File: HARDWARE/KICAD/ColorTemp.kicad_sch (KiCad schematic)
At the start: 29 parts, among them J1 Conn_02x05_Odd_Even, J2 USB_C_Receptacle_PowerOnly_6P, Q1 MMBT3904, Q2 MMBT3904, Q3 MMBT3904, SW1 ~{RESET}, SW2 SW_Push, U1 CH32V003F4U6, U2 MCP9700A

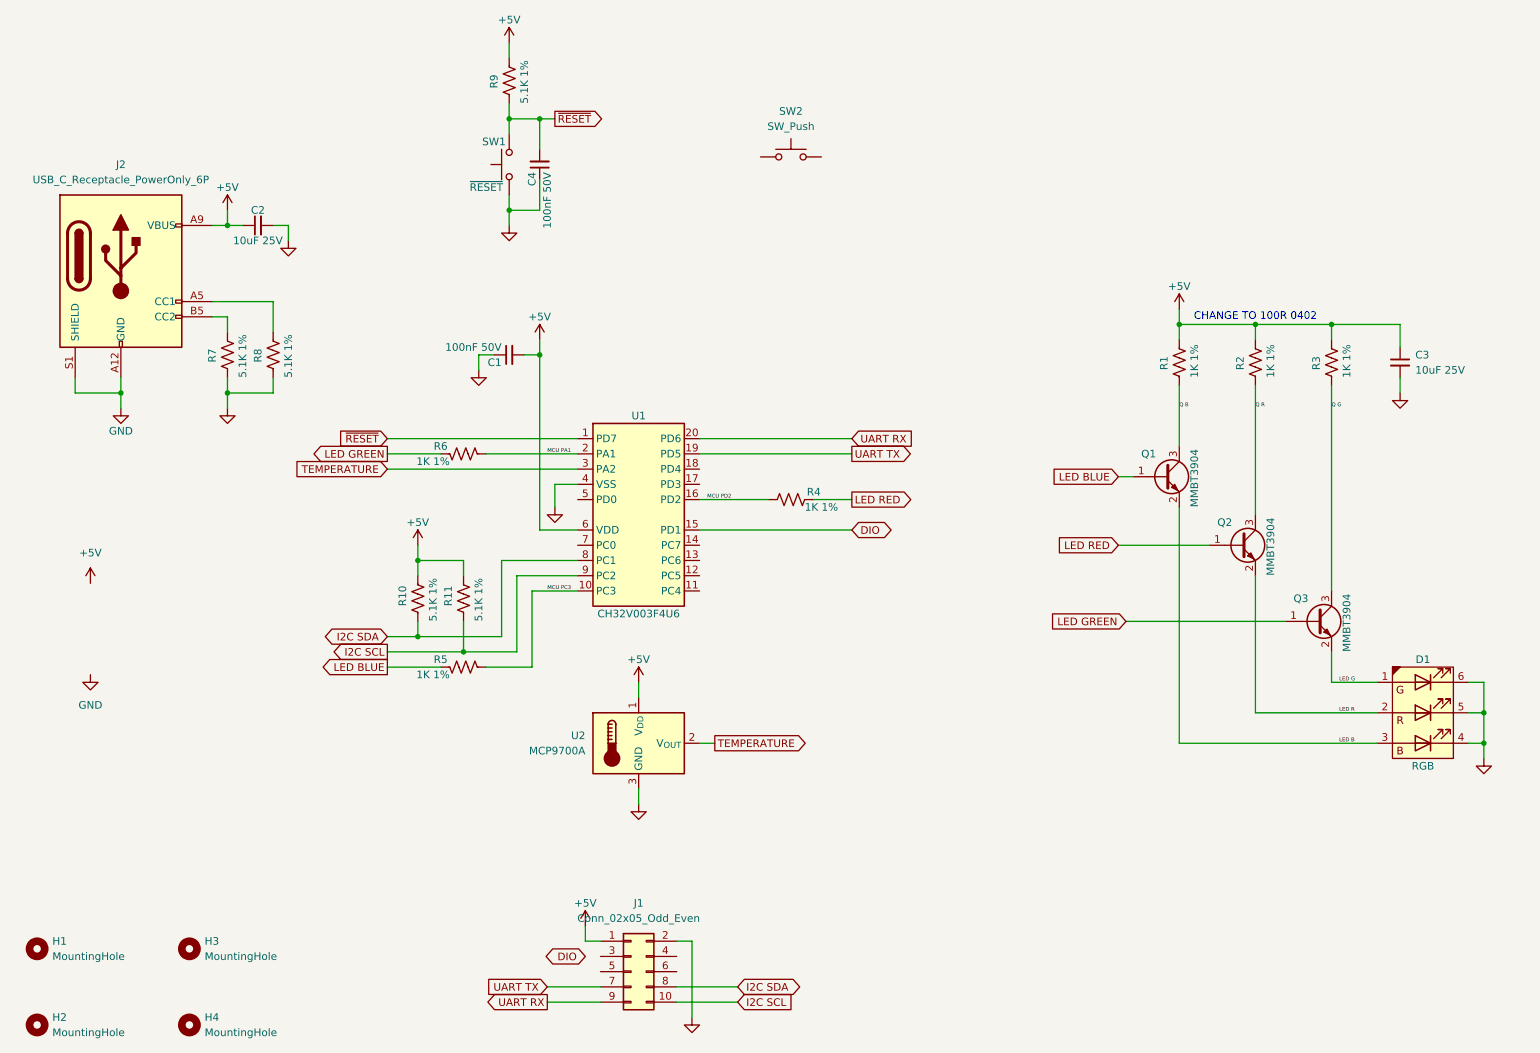
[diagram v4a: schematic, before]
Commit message: Removed transistors for driving LED. Advanced circuit and layout design. Added switches.
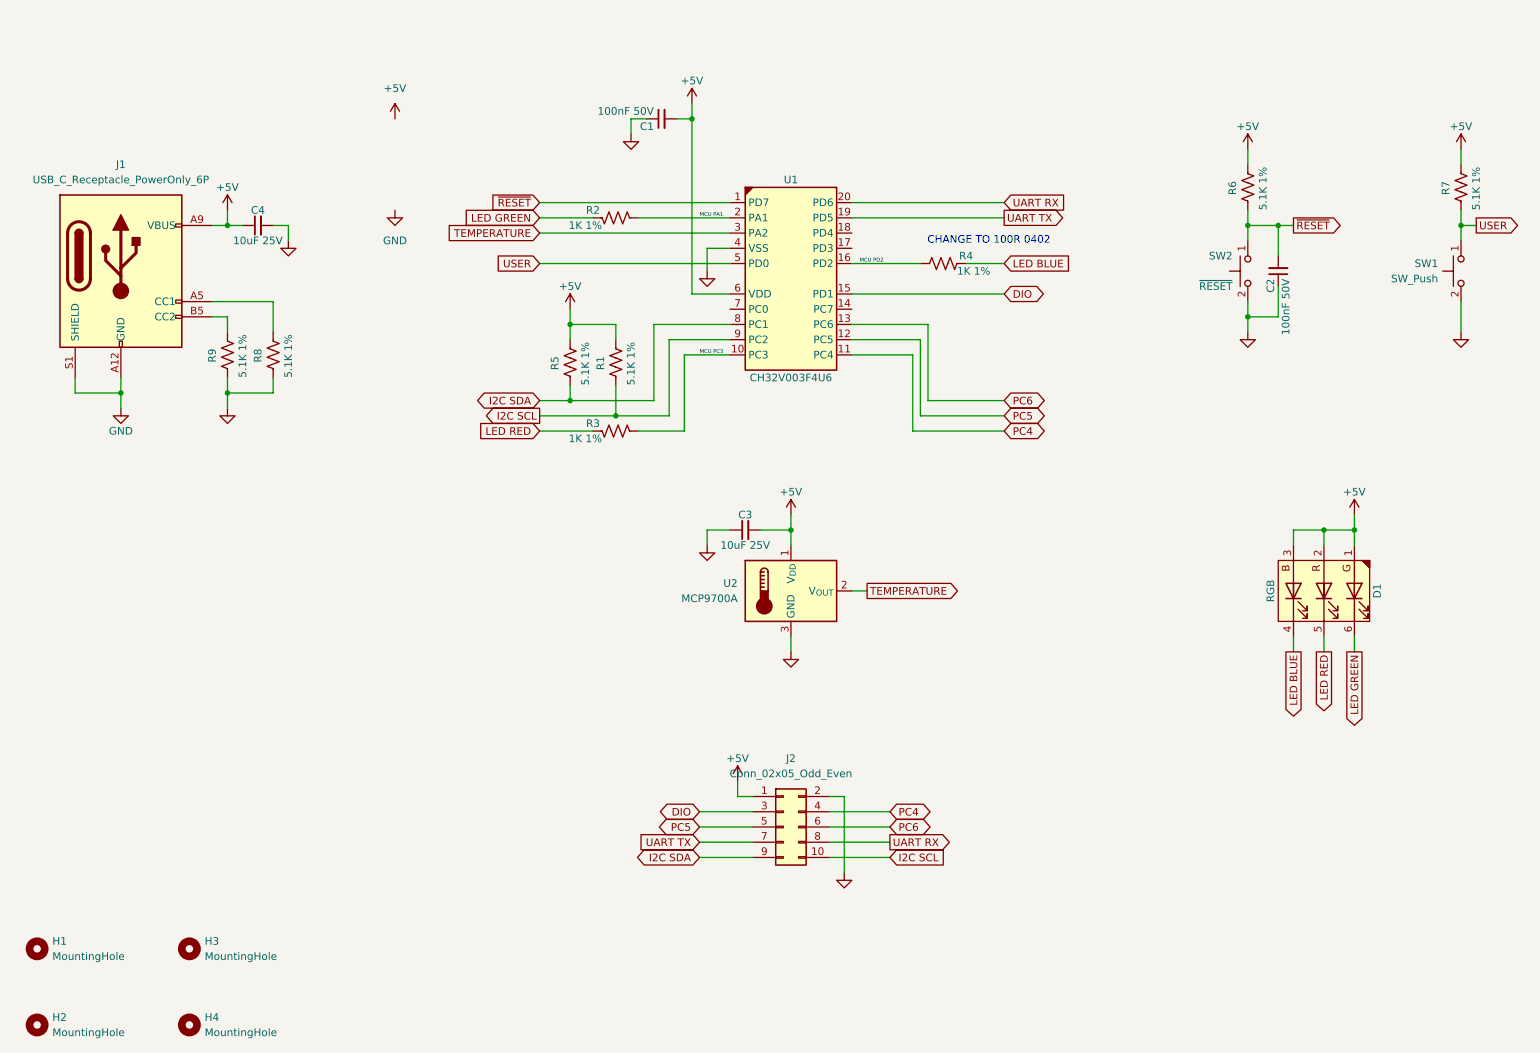
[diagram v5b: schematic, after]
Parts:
- removed Q1, Q2, Q3: MMBT3904, ColorTemp:SOT-23, symbol ColorTemp:MMBT3904
- removed R1, R2, R3: 1K 1%, ColorTemp:R_0603_1608Metric, symbol ColorTemp:R0603 1K 1% 75V 100mW
- removed SW1: ~{RESET}, symbol ColorTemp:SW_Push
- removed SW2: SW_Push, symbol ColorTemp:SW_Push
- added R7: 5.1K 1%, ColorTemp:R_0402_1005Metric, symbol ColorTemp:R0402 5.1K 1% 50V 62.5mW
- added SW1: SW_Push, ColorTemp:EVQP7A01P, symbol ColorTemp: EVQP7A01P
- added SW2: ~{RESET}, ColorTemp:EVQP7A01P, symbol ColorTemp: EVQP7A01P
- renumbered C4 to C2, C2 to C4, J2 to J1, J1 to J2, R11 to R1, R6 to R2, R5 to R3, R10 to R5, R9 to R6, R7 to R9
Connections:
- net LED B is gone; now on net +5V: D1.3 (A)
- net LED G is gone; now on net +5V: D1.1 (A)
- net LED R is gone; now on net +5V: D1.2 (A)
- net +5V: now also C3.2, R7.1; no longer C3.1
- net DIO: now also J2.3 (Pin_3)
- net GND: now also C3.1, SW1.2, SW2.2; no longer C3.2, D1.4 (K), D1.5 (K), D1.6 (K)
- net I2C SDA: now also J2.9 (Pin_9); no longer J2.8 (Pin_8)
- net LED BLUE: now also D1.4 (K), R4.2; no longer R3.2
- net LED GREEN: now also D1.6 (K)
- net LED RED: now also D1.5 (K), R3.2; no longer R4.2
- net UART RX: now also J2.8 (Pin_8); no longer J2.9 (Pin_9)
- net ~{RESET}: now also SW2.1
- net PC4: now reaches J2.4 (Pin_4)
- net PC4: now also U1.11 (PC4)
- net PC5: now reaches J2.5 (Pin_5)
- net PC5: now also U1.12 (PC5)
- net PC6: now reaches J2.6 (Pin_6)
- net PC6: now also U1.13 (PC6)
- net USER: now reaches U1.5 (PD0)
- net USER: now also R7.2, SW1.1
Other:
- moved on the sheet: C1, C2, D1, J2, R1, R2, R3, R4, R5, R6, U2

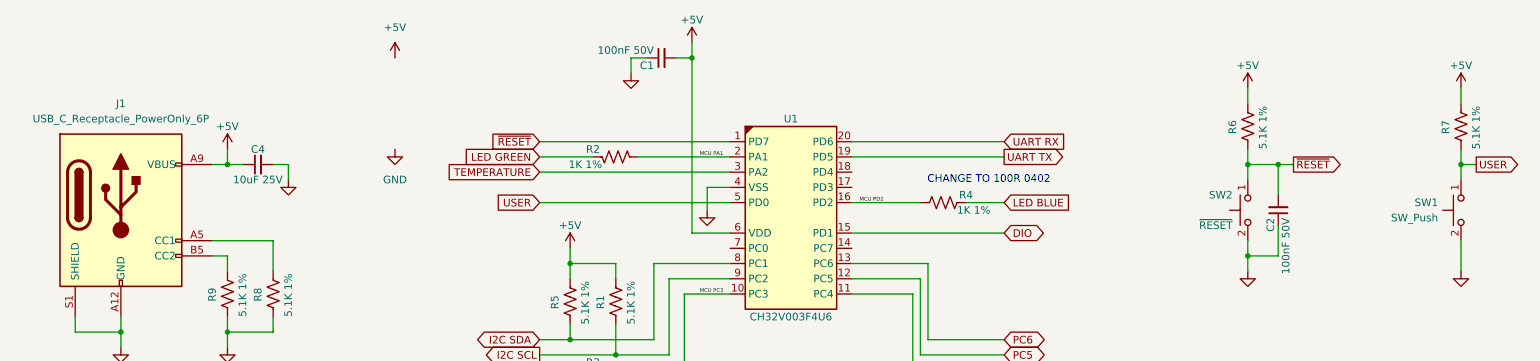
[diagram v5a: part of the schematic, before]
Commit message: Detailing layout and silkscreen.
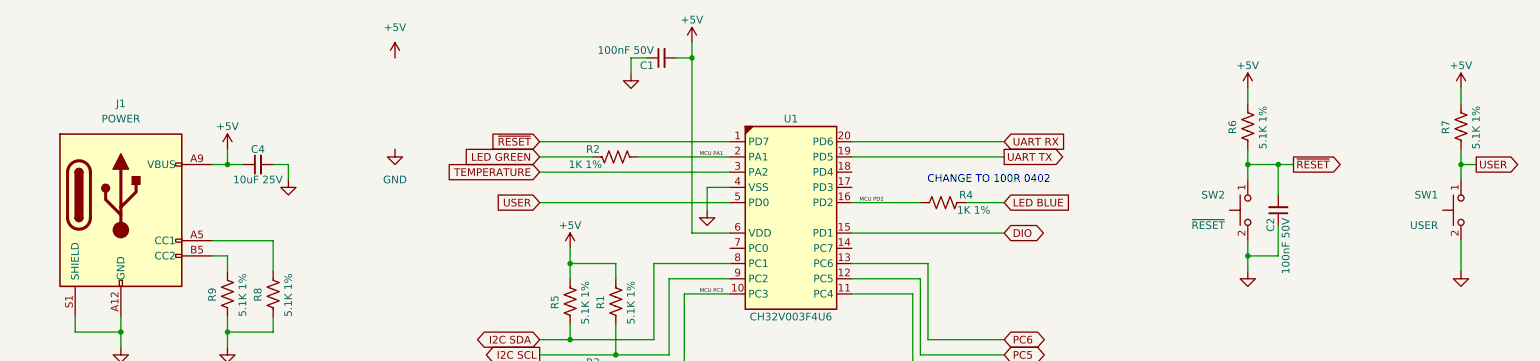
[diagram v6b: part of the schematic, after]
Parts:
- J1: value USB_C_Receptacle_PowerOnly_6P -> POWER
- SW1: value SW_Push -> USER
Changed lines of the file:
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@@
 		(dnp no)
 		(property "Reference" "SW1"
-			(at 260.35 59.6899 90)
+			(at 260.35 58.42 90)
 			(effects
 				(font
@@
 			)
 		)
-		(property "Value" "SW_Push"
-			(at 260.35 62.2299 90)
+		(property "Value" "USER"
+			(at 260.35 63.5 90)
 			(effects
 				(font
@@
 			)
 		)
-		(property "Value" "USB_C_Receptacle_PowerOnly_6P"
+		(property "Value" "POWER"
 			(at 40.64 45.72 0)
 			(effects
@@
 		(dnp no)
 		(property "Reference" "SW2"
-			(at 226.06 58.42 90)
+			(at 224.79 58.42 90)
 			(effects
 				(font
@@
 		)
 		(property "Value" "~{RESET}"
-			(at 226.06 63.5 90)
-			(effects
-				(font
+			(at 224.79 63.5 90)
+			(effects
+				(font

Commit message: Added fiducial marks.
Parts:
- added FID1, FID2, FID3: Fiducial, ColorTemp:Fiducial_0.5mm_Mask1mm, symbol ColorTemp:Fiducial
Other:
- moved on the sheet: H1, H2, H3, H4
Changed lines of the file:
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@@
 	(symbol
 		(lib_id "ColorTemp:MountingHole")
-		(at 52.07 186.69 0)
+		(at 50.8 177.8 0)
 		(unit 1)
 		(exclude_from_sim no)
@@
 		(fields_autoplaced yes)
 		(property "Reference" "H4"
-			(at 54.61 185.4199 0)
+			(at 53.34 176.5299 0)
 			(effects
 				(font
@@
 		)
 		(property "Value" "MountingHole"
-			(at 54.61 187.9599 0)
+			(at 53.34 179.0699 0)
 			(effects
 				(font
@@
 		)
 		(property "Footprint" "ColorTemp:MountingHole_3.2mm_M3"
-			(at 52.07 186.69 0)
+			(at 50.8 177.8 0)
 			(effects
 				(font
@@
 		)
 		(property "Datasheet" "~"
-			(at 52.07 186.69 0)
+			(at 50.8 177.8 0)
 			(effects
 				(font
@@
 		)
 		(property "Description" "Mounting Hole without connection"
-			(at 52.07 186.69 0)
+			(at 50.8 177.8 0)
 			(effects
 				(font
@@
 	(symbol
 		(lib_id "ColorTemp:MountingHole")
-		(at 26.67 186.69 0)
+		(at 25.4 177.8 0)
 		(unit 1)
 		(exclude_from_sim no)
@@
 		(fields_autoplaced yes)
 		(property "Reference" "H2"
-			(at 29.21 185.4199 0)
+			(at 27.94 176.5299 0)
 			(effects
 				(font
@@
 		)
 		(property "Value" "MountingHole"
-			(at 29.21 187.9599 0)
+			(at 27.94 179.0699 0)
 			(effects
 				(font
@@
 		)
 		(property "Footprint" "ColorTemp:MountingHole_3.2mm_M3"
-			(at 26.67 186.69 0)
+			(at 25.4 177.8 0)
 			(effects
 				(font
@@
 		)
 		(property "Datasheet" "~"
-			(at 26.67 186.69 0)
+			(at 25.4 177.8 0)
 			(effects
 				(font
@@
 		)
 		(property "Description" "Mounting Hole without connection"
-			(at 26.67 186.69 0)
+			(at 25.4 177.8 0)
 			(effects
 				(font
@@
 	)
 	(symbol
+		(lib_id "ColorTemp:Fiducial")
+		(at 25.4 152.4 0)
+		(unit 1)
+		(exclude_from_sim no)
+		(in_bom no)
+		(on_board yes)
+		(dnp no)
+		(fields_autoplaced yes)
+		(property "Reference" "FID2"
+			(at 27.94 151.1299 0)
+			(effects
+				(font
+					(size 1.27 1.27)
+				)
+				(justify left)
+			)
+		)
+		(property "Value" "Fiducial"
+			(at 27.94 153.6699 0)
+			(effects
+				(font
+					(size 1.27 1.27)
+				)
+				(justify left)
+			)
+		)
+		(property "Footprint" "ColorTemp:Fiducial_0.5mm_Mask1mm"
+			(at 25.4 152.4 0)
+			(effects
+				(font
+					(size 1.27 1.27)
+				)
+				(hide yes)
+			)
+		)
+		(property "Datasheet" "~"
+			(at 25.4 152.4 0)
+			(effects
+				(font
+					(size 1.27 1.27)
+				)
+				(hide yes)
+			)
+		)
+		(property "Description" "Fiducial Marker"
+			(at 25.4 152.4 0)
+			(effects
+				(font
+					(size 1.27 1.27)
+				)
+				(hide yes)
+			)
+		)
+		(instances
+			(project "ColorTemp"
+				(path "/b6e9e66b-bd82-486a-892a-2943c5ea8e95"
+					(reference "FID2")
+					(unit 1)
+				)
+			)
+		)
+	)
+	(symbol
 		(lib_id "ColorTemp:+5V")
 		(at 228.6 40.64 0)
@@
 				(path "/b6e9e66b-bd82-486a-892a-2943c5ea8e95"
 					(reference "J1")
+					(unit 1)
+				)
+			)
+		)
+	)
+	(symbol
+		(lib_id "ColorTemp:Fiducial")
+		(at 25.4 139.7 0)
+		(unit 1)
+		(exclude_from_sim no)
+		(in_bom no)
+		(on_board yes)
+		(dnp no)
+		(fields_autoplaced yes)
+		(property "Reference" "FID1"
+			(at 27.94 138.4299 0)
+			(effects
+				(font
+					(size 1.27 1.27)
+				)
+				(justify left)
+			)
+		)
+		(property "Value" "Fiducial"
+			(at 27.94 140.9699 0)
+			(effects
+				(font
+					(size 1.27 1.27)
+				)
+				(justify left)
+			)
+		)
+		(property "Footprint" "ColorTemp:Fiducial_0.5mm_Mask1mm"
+			(at 25.4 139.7 0)
+			(effects
+				(font
+					(size 1.27 1.27)
+				)
+				(hide yes)
+			)
+		)
+		(property "Datasheet" "~"
+			(at 25.4 139.7 0)
+			(effects
+				(font
+					(size 1.27 1.27)
+				)
+				(hide yes)
+			)
+		)
+		(property "Description" "Fiducial Marker"
+			(at 25.4 139.7 0)
+			(effects
+				(font
+					(size 1.27 1.27)
+				)
+				(hide yes)
+			)
+		)
+		(instances
+			(project ""
+				(path "/b6e9e66b-bd82-486a-892a-2943c5ea8e95"
+					(reference "FID1")
 					(unit 1)
 				)
@@
 	(symbol
 		(lib_id "ColorTemp:MountingHole")
-		(at 26.67 173.99 0)
+		(at 25.4 165.1 0)
 		(unit 1)
 		(exclude_from_sim no)
@@
 		(fields_autoplaced yes)
 		(property "Reference" "H1"
-			(at 29.21 172.7199 0)
+			(at 27.94 163.8299 0)
 			(effects
 				(font
@@
 		)
 		(property "Value" "MountingHole"
-			(at 29.21 175.2599 0)
+			(at 27.94 166.3699 0)
 			(effects
 				(font
@@
 		)
 		(property "Footprint" "ColorTemp:MountingHole_3.2mm_M3"
-			(at 26.67 173.99 0)
+			(at 25.4 165.1 0)
 			(effects
 				(font
@@
 		)
 		(property "Datasheet" "~"
-			(at 26.67 173.99 0)
+			(at 25.4 165.1 0)
 			(effects
 				(font
@@
 		)
 		(property "Description" "Mounting Hole without connection"
-			(at 26.67 173.99 0)
+			(at 25.4 165.1 0)
 			(effects
 				(font
@@
 	(symbol
 		(lib_id "ColorTemp:MountingHole")
-		(at 52.07 173.99 0)
+		(at 50.8 165.1 0)
 		(unit 1)
 		(exclude_from_sim no)
@@
 		(fields_autoplaced yes)
 		(property "Reference" "H3"
-			(at 54.61 172.7199 0)
+			(at 53.34 163.8299 0)
 			(effects
 				(font
@@
 		)
 		(property "Value" "MountingHole"
-			(at 54.61 175.2599 0)
+			(at 53.34 166.3699 0)
 			(effects
 				(font
@@
 		)
 		(property "Footprint" "ColorTemp:MountingHole_3.2mm_M3"
-			(at 52.07 173.99 0)
+			(at 50.8 165.1 0)
 			(effects
 				(font
@@
 		)
 		(property "Datasheet" "~"
-			(at 52.07 173.99 0)
+			(at 50.8 165.1 0)
 			(effects
 				(font
@@
 		)
 		(property "Description" "Mounting Hole without connection"
-			(at 52.07 173.99 0)
+			(at 50.8 165.1 0)
 			(effects
 				(font
@@
 					(unit 1)
 				)
+			)
+		)
+	)
+	(symbol
+		(lib_id "ColorTemp:Fiducial")
+		(at 50.8 152.4 0)
+		(unit 1)
+		(exclude_from_sim no)
+		(in_bom no)
+		(on_board yes)
+		(dnp no)
+		(fields_autoplaced yes)
+		(property "Reference" "FID3"
+			(at 53.34 151.1299 0)
+			(effects
+				(font
+					(size 1.27 1.27)
+				)
+				(justify left)
+			)
+		)
+		(property "Value" "Fiducial"
+			(at 53.34 153.6699 0)
+			(effects
+				(font
+					(size 1.27 1.27)
+				)
+				(justify left)
+			)
+		)
+		(property "Footprint" "ColorTemp:Fiducial_0.5mm_Mask1mm"
+			(at 50.8 152.4 0)
+			(effects
+				(font
+					(size 1.27 1.27)
+				)
+				(hide yes)
+			)
+		)
+		(property "Datasheet" "~"
+			(at 50.8 152.4 0)
+			(effects
+				(font
+					(size 1.27 1.27)
+				)
+				(hide yes)
+			)
+		)
+		(property "Description" "Fiducial Marker"
+			(at 50.8 152.4 0)
+			(effects
+				(font
+					(size 1.27 1.27)
+				)
+				(hide yes)
+			)
+		)
+		(instances
+			(project "ColorTemp"
+				(path "/b6e9e66b-bd82-486a-892a-2943c5ea8e95"
+					(reference "FID3")
+					(unit 1)
+				)
